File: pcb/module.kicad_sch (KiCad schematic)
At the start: 1 part

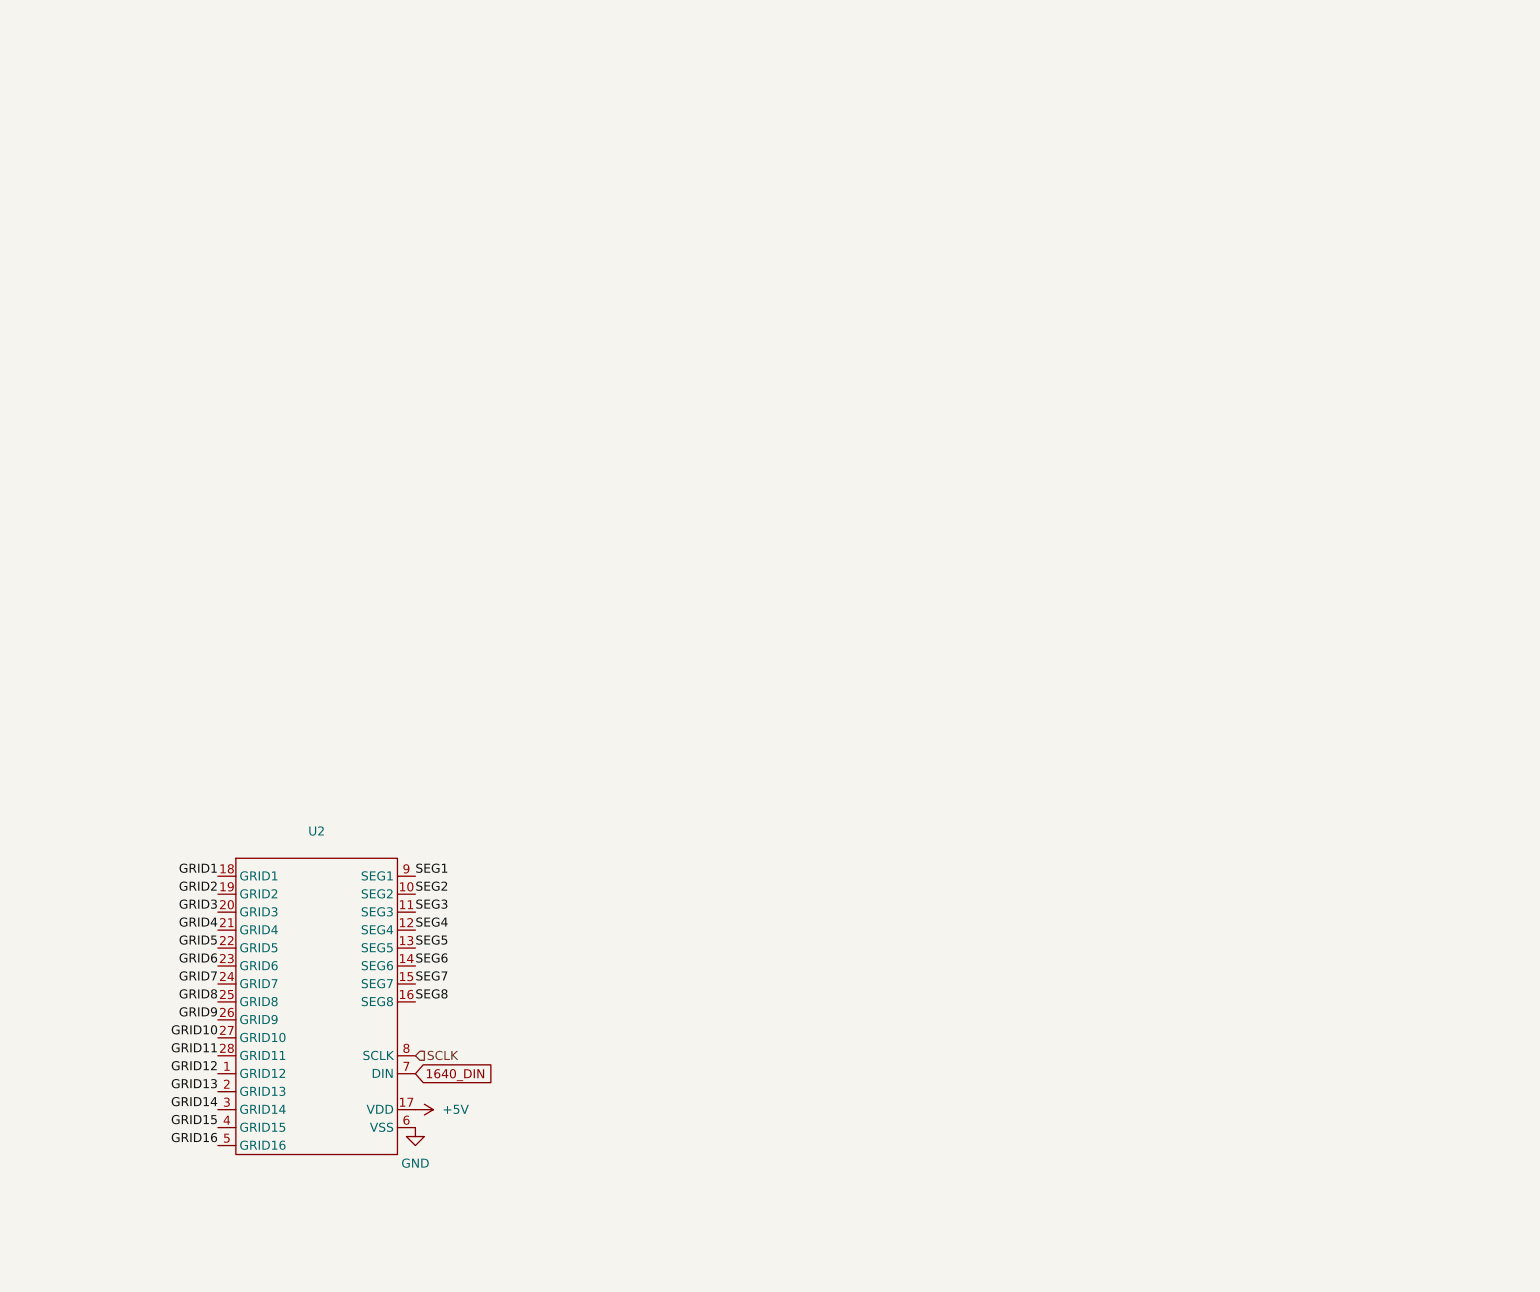
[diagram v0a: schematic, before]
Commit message: add displays to module subsheet
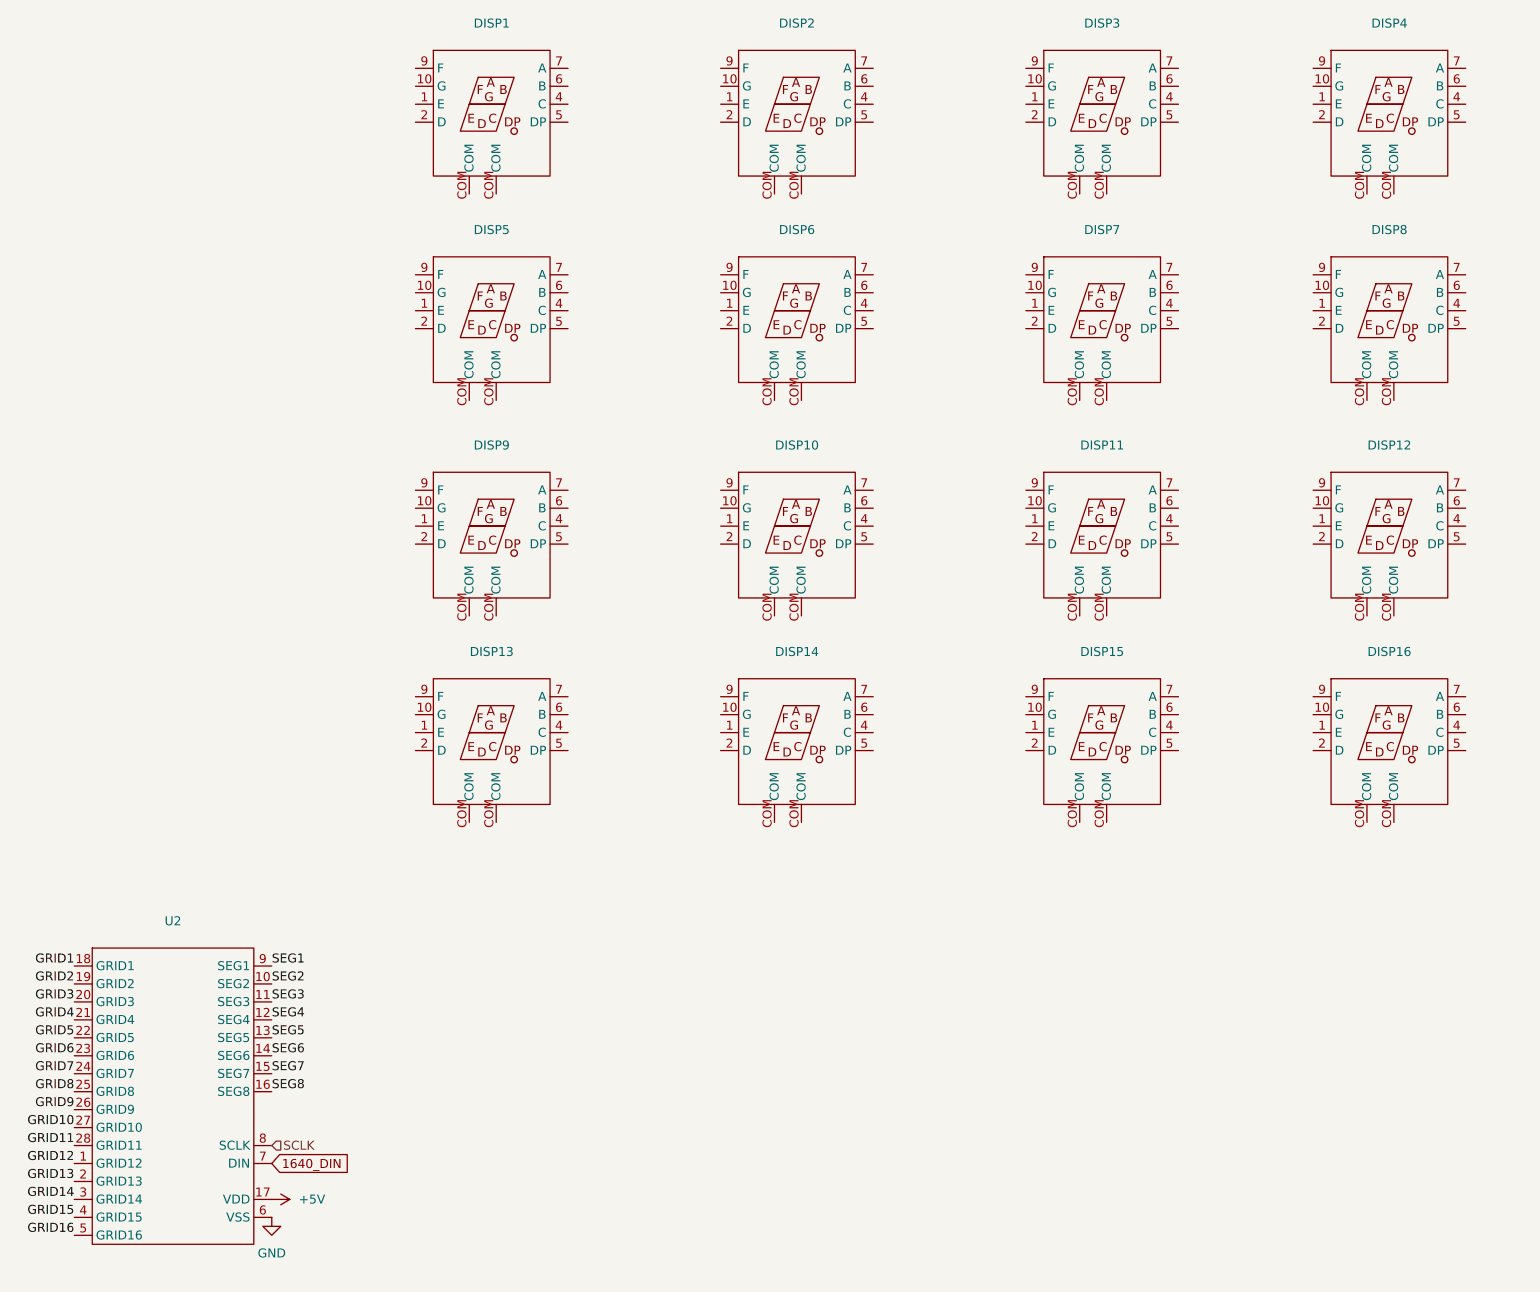
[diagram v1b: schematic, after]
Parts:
- added DISP1, DISP10, DISP11, DISP12, DISP13, DISP14, DISP15, DISP16, DISP2, DISP3, DISP4, DISP5, DISP6, DISP7, DISP8, DISP9: ~, ssdd:5611BH, symbol ssdd:5611BH
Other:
- moved on the sheet: U2

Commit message: connect segment pins in module
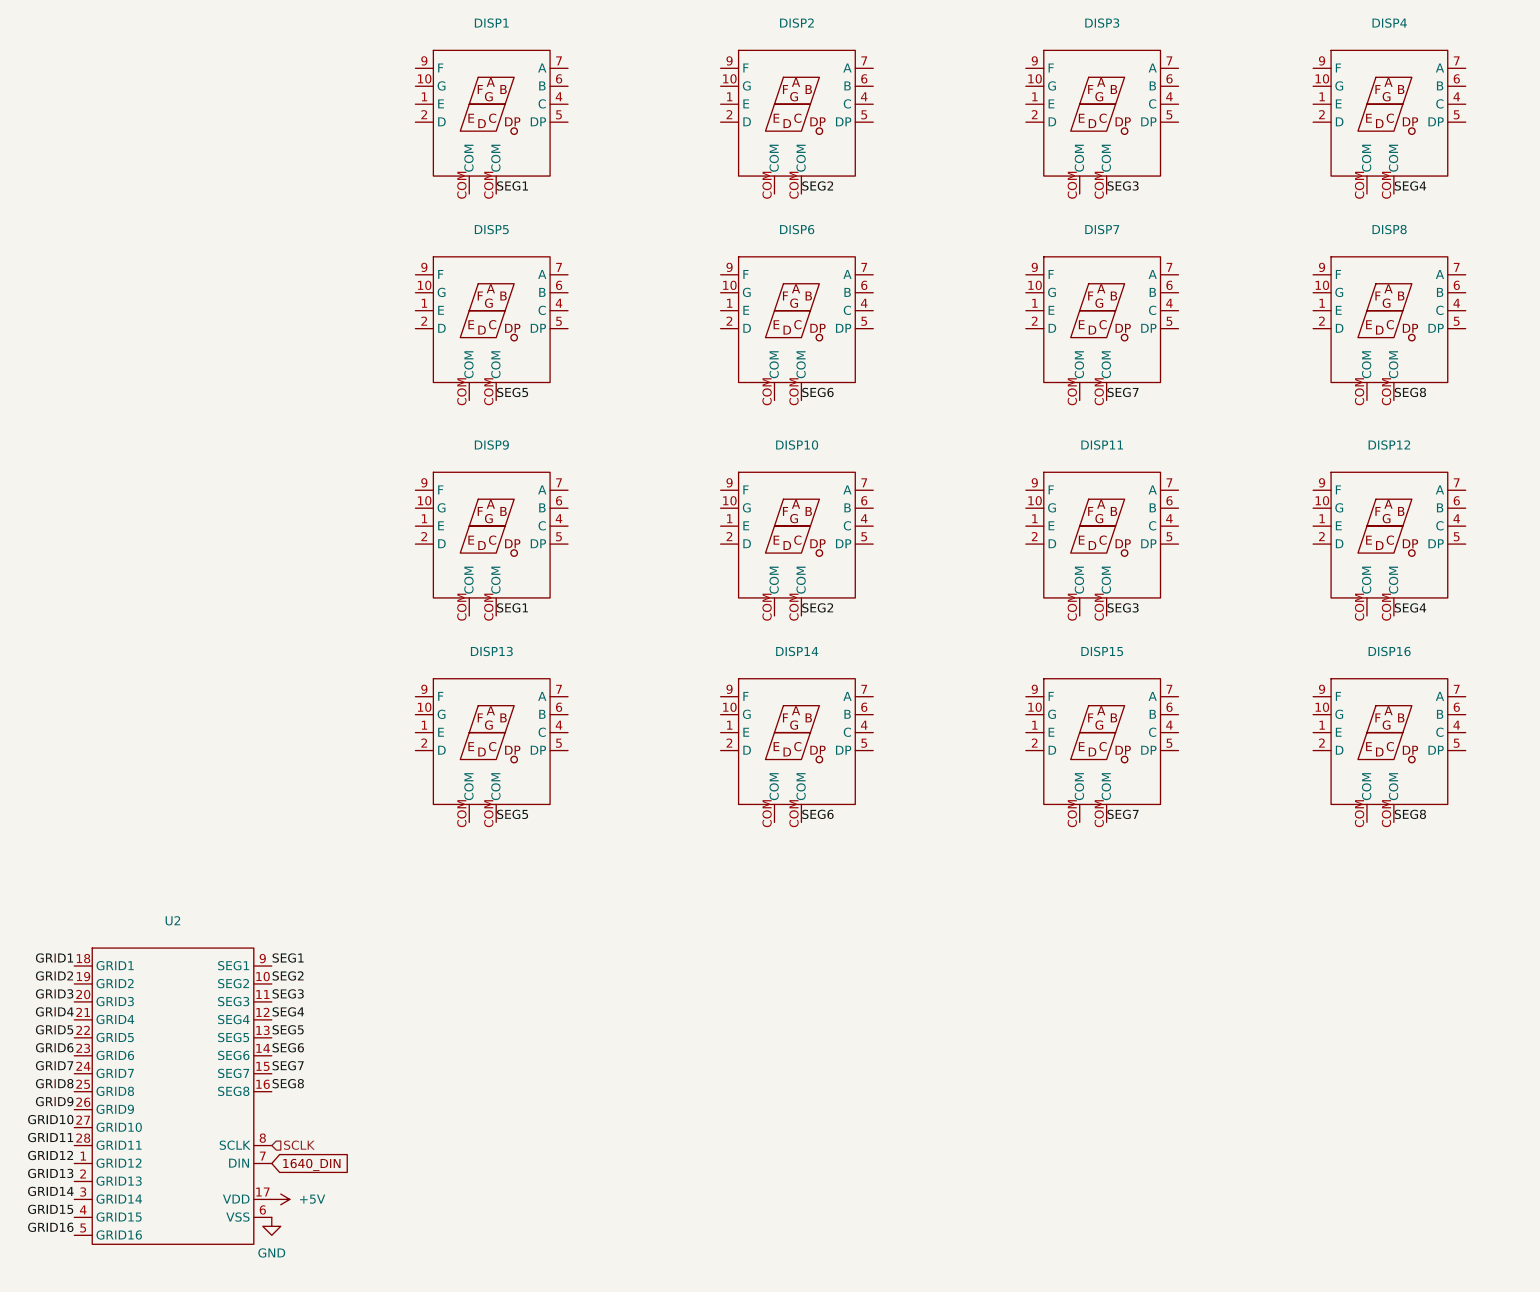
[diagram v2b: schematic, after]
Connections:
- net SEG1: now also DISP1.COM, DISP9.COM
- net SEG2: now also DISP10.COM, DISP2.COM
- net SEG3: now also DISP11.COM, DISP3.COM
- net SEG4: now also DISP12.COM, DISP4.COM
- net SEG5: now also DISP13.COM, DISP5.COM
- net SEG6: now also DISP14.COM, DISP6.COM
- net SEG7: now also DISP15.COM, DISP7.COM
- net SEG8: now also DISP16.COM, DISP8.COM
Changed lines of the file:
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@@
 	(generator_version "9.0")
 	(paper "A4")
+	(label "SEG2"
+		(at 125.73 105.41 0)
+		(effects
+			(font
+				(size 1.27 1.27)
+			)
+			(justify left bottom)
+		)
+	)
+	(label "SEG4"
+		(at 209.55 45.72 0)
+		(effects
+			(font
+				(size 1.27 1.27)
+			)
+			(justify left bottom)
+		)
+	)
 	(label "GRID6"
 		(at 22.86 167.64 180)
@@
 		)
 	)
+	(label "SEG8"
+		(at 209.55 74.93 0)
+		(effects
+			(font
+				(size 1.27 1.27)
+			)
+			(justify left bottom)
+		)
+	)
 	(label "GRID13"
 		(at 22.86 185.42 180)
@@
 		)
 	)
+	(label "SEG8"
+		(at 209.55 134.62 0)
+		(effects
+			(font
+				(size 1.27 1.27)
+			)
+			(justify left bottom)
+		)
+	)
+	(label "SEG1"
+		(at 82.55 105.41 0)
+		(effects
+			(font
+				(size 1.27 1.27)
+			)
+			(justify left bottom)
+		)
+	)
 	(label "SEG5"
 		(at 50.8 165.1 0)
@@
 		)
 	)
+	(label "SEG2"
+		(at 125.73 45.72 0)
+		(effects
+			(font
+				(size 1.27 1.27)
+			)
+			(justify left bottom)
+		)
+	)
+	(label "SEG1"
+		(at 82.55 45.72 0)
+		(effects
+			(font
+				(size 1.27 1.27)
+			)
+			(justify left bottom)
+		)
+	)
 	(label "GRID1"
 		(at 22.86 154.94 180)
@@
 		)
 	)
+	(label "SEG7"
+		(at 168.91 74.93 0)
+		(effects
+			(font
+				(size 1.27 1.27)
+			)
+			(justify left bottom)
+		)
+	)
 	(label "GRID14"
 		(at 22.86 187.96 180)
@@
 	)
 	(label "SEG6"
+		(at 125.73 74.93 0)
+		(effects
+			(font
+				(size 1.27 1.27)
+			)
+			(justify left bottom)
+		)
+	)
+	(label "SEG5"
+		(at 82.55 134.62 0)
+		(effects
+			(font
+				(size 1.27 1.27)
+			)
+			(justify left bottom)
+		)
+	)
+	(label "SEG6"
 		(at 50.8 167.64 0)
+		(effects
+			(font
+				(size 1.27 1.27)
+			)
+			(justify left bottom)
+		)
+	)
+	(label "SEG7"
+		(at 168.91 134.62 0)
+		(effects
+			(font
+				(size 1.27 1.27)
+			)
+			(justify left bottom)
+		)
+	)
+	(label "SEG3"
+		(at 168.91 105.41 0)
+		(effects
+			(font
+				(size 1.27 1.27)
+			)
+			(justify left bottom)
+		)
+	)
+	(label "SEG4"
+		(at 209.55 105.41 0)
 		(effects
 			(font
@@
 		)
 	)
+	(label "SEG3"
+		(at 168.91 45.72 0)
+		(effects
+			(font
+				(size 1.27 1.27)
+			)
+			(justify left bottom)
+		)
+	)
 	(label "GRID10"
 		(at 22.86 177.8 180)
@@
 		)
 	)
+	(label "SEG5"
+		(at 82.55 74.93 0)
+		(effects
+			(font
+				(size 1.27 1.27)
+			)
+			(justify left bottom)
+		)
+	)
+	(label "SEG6"
+		(at 125.73 134.62 0)
+		(effects
+			(font
+				(size 1.27 1.27)
+			)
+			(justify left bottom)
+		)
+	)

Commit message: grid1-grid8
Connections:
- net GRID1: now also DISP1.7 (A), DISP2.7 (A), DISP3.7 (A), DISP4.7 (A), DISP5.7 (A), DISP6.7 (A), DISP7.7 (A), DISP8.7 (A)
- net GRID2: now also DISP1.6 (B), DISP2.6 (B), DISP3.6 (B), DISP4.6 (B), DISP5.6 (B), DISP6.6 (B), DISP7.6 (B), DISP8.6 (B)
- net GRID3: now also DISP1.4 (C), DISP2.4 (C), DISP3.4 (C), DISP4.4 (C), DISP5.4 (C), DISP6.4 (C), DISP7.4 (C), DISP8.4 (C)
- net GRID4: now also DISP1.2 (D), DISP2.2 (D), DISP3.2 (D), DISP4.2 (D), DISP5.2 (D), DISP6.2 (D), DISP7.2 (D), DISP8.2 (D)
- net GRID5: now also DISP1.1 (E), DISP2.1 (E), DISP3.1 (E), DISP4.1 (E), DISP5.1 (E), DISP6.1 (E), DISP7.1 (E), DISP8.1 (E)
- net GRID6: now also DISP1.10 (G), DISP2.10 (G), DISP3.10 (G), DISP4.10 (G), DISP5.10 (G), DISP6.10 (G), DISP7.10 (G), DISP8.10 (G)
- net GRID7: now also DISP1.9 (F), DISP2.9 (F), DISP3.9 (F), DISP4.9 (F), DISP5.9 (F), DISP6.9 (F), DISP7.9 (F), DISP8.9 (F)
- net GRID8: now also DISP1.5 (DP), DISP2.5 (DP), DISP3.5 (DP), DISP4.5 (DP), DISP5.5 (DP), DISP6.5 (DP), DISP7.5 (DP), DISP8.5 (DP)

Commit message: grid9-grid16
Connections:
- net GRID10: now also DISP10.6 (B), DISP11.6 (B), DISP12.6 (B), DISP13.6 (B), DISP14.6 (B), DISP15.6 (B), DISP16.6 (B), DISP9.6 (B)
- net GRID11: now also DISP10.4 (C), DISP11.4 (C), DISP12.4 (C), DISP13.4 (C), DISP14.4 (C), DISP15.4 (C), DISP16.4 (C), DISP9.4 (C)
- net GRID12: now also DISP10.2 (D), DISP11.2 (D), DISP12.2 (D), DISP13.2 (D), DISP14.2 (D), DISP15.2 (D), DISP16.2 (D), DISP9.2 (D)
- net GRID13: now also DISP10.1 (E), DISP11.1 (E), DISP12.1 (E), DISP13.1 (E), DISP14.1 (E), DISP15.1 (E), DISP16.1 (E), DISP9.1 (E)
- net GRID14: now also DISP10.10 (G), DISP11.10 (G), DISP12.10 (G), DISP13.10 (G), DISP14.10 (G), DISP15.10 (G), DISP16.10 (G), DISP9.10 (G)
- net GRID15: now also DISP10.9 (F), DISP11.9 (F), DISP12.9 (F), DISP13.9 (F), DISP14.9 (F), DISP15.9 (F), DISP16.9 (F), DISP9.9 (F)
- net GRID16: now also DISP10.5 (DP), DISP11.5 (DP), DISP12.5 (DP), DISP13.5 (DP), DISP14.5 (DP), DISP15.5 (DP), DISP16.5 (DP), DISP9.5 (DP)
- net GRID9: now also DISP10.7 (A), DISP11.7 (A), DISP12.7 (A), DISP13.7 (A), DISP14.7 (A), DISP15.7 (A), DISP16.7 (A), DISP9.7 (A)

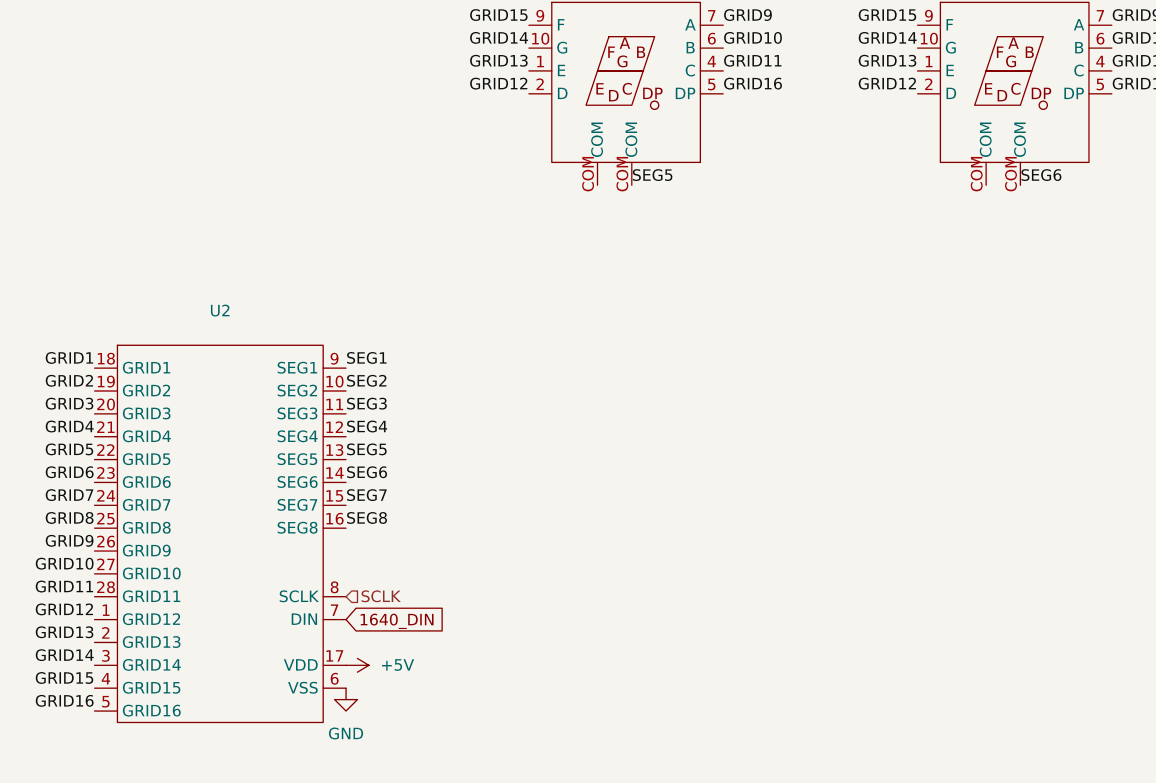
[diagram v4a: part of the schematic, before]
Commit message: tm1640 capacitors according to datasheet
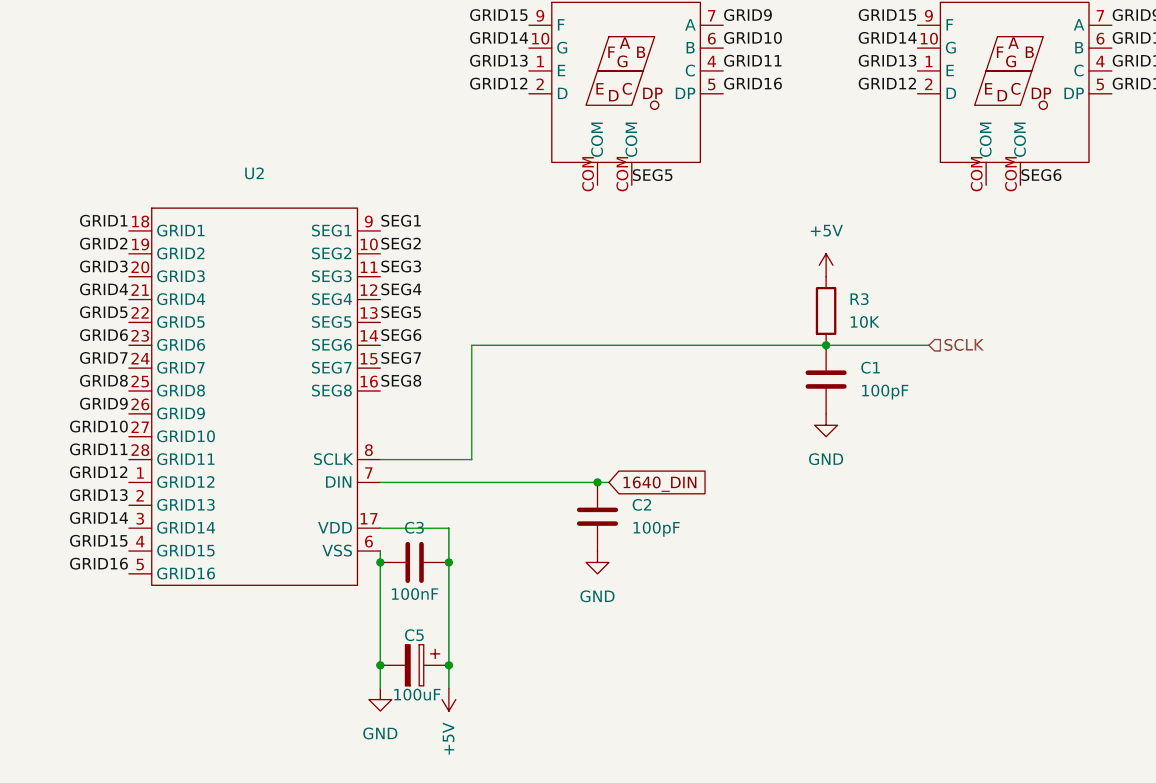
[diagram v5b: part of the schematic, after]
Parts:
- added C1, C2: 100pF, symbol Device:C
- added C3: 100nF, symbol Device:C
- added C5: 100uF, symbol Device:C_Polarized
- added R3: 10K, symbol Device:R
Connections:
- net +5V: now also C3.2, C5.1, R3.1
- net 1640_DIN: now also C2.1
- net GND: now also C1.2, C2.2, C3.1, C5.2
- net SCLK: now also C1.1, R3.2
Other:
- moved on the sheet: U2

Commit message: connect modules
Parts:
- renumbered C1 to C, C5 to C, C3 to C, C2 to C, DISP2 to DISP, DISP4 to DISP, DISP3 to DISP, DISP1 to DISP, R3 to R, U2 to U
